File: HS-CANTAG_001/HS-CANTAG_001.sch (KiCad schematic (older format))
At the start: 20 parts, among them Y1 16MHz

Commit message: ・CANTAG回路図編集
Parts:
- removed J?: B5B-XH-A_LF__SN_, digikey-footprints:PinHeader_1x5_P2.5mm_Drill1.1mm, symbol dk_Rectangular-Connectors-Headers-Male-Pins:B5B-XH-A_LF__SN_
- added C6, C9: 100uf, symbol Device:C
- added C7, C8: 0.1uf, symbol Device:C
- added D1: 5A, Diode_THT:D_DO-41_SOD81_P10.16mm_Horizontal, symbol Diode:SB160
- added J?: B4B-XH-A_LF__SN_, digikey-footprints:PinHeader_1x4_P2.5mm_Drill1.1mm, symbol dk_Rectangular-Connectors-Headers-Male-Pins:B4B-XH-A_LF__SN_
- added J?: Jack-DC, symbol Connector:Jack-DC
- added SW?: SW_Push, symbol Switch:SW_Push
- added U?: R-78E5.0-0.5, Converter_DCDC:Converter_DCDC_RECOM_R-78E-0.5_THT, symbol Regulator_Switching:R-78E5.0-0.5
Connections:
- wire segments 84 -> 104
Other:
- moved on the sheet: C1, C2, C3, C4, C5, CAN_H, D1, J?, JP?, R1, R2, R3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

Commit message: ・CAN回路更新
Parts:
- removed J?: Jack-DC, symbol Connector:Jack-DC
- added J3: Barrel_Jack, digikey-footprints:Barrel_Jack_5.5mmODx2.1mmID_PJ-202A, symbol Connector:Barrel_Jack_Switch
- C1, C2, C5, C7, C8: footprint (none) -> Capacitor_SMD:C_1206_3216Metric
- C3, C4: footprint (none) -> Capacitor_THT:C_Disc_D4.3mm_W1.9mm_P5.00mm
- C6, C9: footprint (none) -> Capacitor_THT:CP_Radial_D6.3mm_P2.50mm
- CAN_H1: renamed from CAN_H; footprint digikey-footprints:PinHeader_1x2_P2mm_Drill1mm -> Connector_PinSocket_2.54mm:PinSocket_1x02_P2.54mm_Vertical
- D1: footprint (none) -> digikey-footprints:LED_3mm_Radial
- J1: renamed from J?; footprint digikey-footprints:PinHeader_1x2_P2mm_Drill1mm -> Connector_PinHeader_2.54mm:PinHeader_1x02_P2.54mm_Vertical
- J2: renamed from J?; footprint digikey-footprints:PinHeader_1x4_P2.5mm_Drill1.1mm -> Connector_PinHeader_2.54mm:PinHeader_1x04_P2.54mm_Vertical
- J4, J5: renamed from J?; footprint digikey-footprints:PinHeader_1x4_P2.5mm_Drill1.1mm -> Connector_Hirose:Hirose_DF63-4P-3.96DSA_1x04_P3.96mm_Horizontal
- JP1: renamed from JP?; footprint (none) -> Connector_PinHeader_2.54mm:PinHeader_1x02_P2.54mm_Vertical
- R1, R2, R3, R4: footprint (none) -> Resistor_THT:R_Axial_DIN0204_L3.6mm_D1.6mm_P7.62mm_Horizontal
- SW1: renamed from SW?; footprint (none) -> digikey-footprints:Switch_Tactile_THT_B3F-1xxx
- U1: renamed from U?; footprint (none) -> hotsprings-footprints:MCP2515_SMD
- U3: renamed from U?; footprint (none) -> hotsprings-footprints:MCP2551_SMD
- Y1: footprint (none) -> Crystal:Crystal_HC49-4H_Vertical
- gave numbers to parts that had none: 1
- renumbered D1 to D2
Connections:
- wire segments 104 -> 105
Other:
- note added: "Power"
- moved on the sheet: C1, C2, C3, C4, C5, C6, C7, C8, C9, CAN_H1, D1, D2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

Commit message: ・回路修正
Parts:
- J4, J5: footprint Connector_Hirose:Hirose_DF63-4P-3.96DSA_1x04_P3.96mm_Horizontal -> Connector_JST:JST_VH_B4P-VH-B_1x04_P3.96mm_Vertical
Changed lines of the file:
@@
 F 0 "J4" V 4991 3172 50  0000 R CNN
 F 1 "CAN1" V 4900 3172 50  0000 R CNN
-F 2 "Connector_Hirose:Hirose_DF63-4P-3.96DSA_1x04_P3.96mm_Horizontal" H 5000 3500 60  0001 L CNN
+F 2 "Connector_JST:JST_VH_B4P-VH-B_1x04_P3.96mm_Vertical" H 5000 3500 60  0001 L CNN
 F 3 "http://www.jst-mfg.com/product/pdf/eng/eXH.pdf" H 5000 3600 60  0001 L CNN
 F 4 "455-2249-ND" H 5000 3700 60  0001 L CNN "Digi-Key_PN"
@@
 F 0 "J5" V 4991 3772 50  0000 R CNN
 F 1 "CAN2" V 4900 3772 50  0000 R CNN
-F 2 "Connector_Hirose:Hirose_DF63-4P-3.96DSA_1x04_P3.96mm_Horizontal" H 5000 4100 60  0001 L CNN
+F 2 "Connector_JST:JST_VH_B4P-VH-B_1x04_P3.96mm_Vertical" H 5000 4100 60  0001 L CNN
 F 3 "http://www.jst-mfg.com/product/pdf/eng/eXH.pdf" H 5000 4200 60  0001 L CNN
 F 4 "455-2249-ND" H 5000 4300 60  0001 L CNN "Digi-Key_PN"

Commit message: ・CAN回路更新
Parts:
- removed U1: MCP2515, hotsprings-footprints:MCP2515_SMD, symbol HotSprings:MCP2515
- added U1: MCP2515_SMD18p, hotsprings-footprints:MCP2515_SMD(18p), symbol HotSprings:MCP2515_SMD18p
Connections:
- net +5V: now also U1.18 (VDD)
- net GNDPWR: now also U1.9 (VSS)
- net at U3.1 (TXD): now also U1.1 (TXCAN)
- net at D1.2 (A): now also U1.11 (RX0BF)
- net at J2.1, RN1.2 (R1): now also U1.13 (SCK)
- net at J2.2, RN1.3 (R2): now also U1.14 (SI)
- net at J2.3, RN1.4 (R3): now also U1.15 (SO)
- net at J2.4, RN1.5 (R4): now also U1.16 (CS)
- net at R1.2, SW1.2: now also U1.17 (RESET)
- net at U3.4 (RXD): now also U1.2 (RXCAN)
- net at C3.1, Y1.1: now also U1.7 (OSC2)
- net at C4.1, Y1.2: now also U1.8 (OSC1)
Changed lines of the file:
@@
 CAN
-$Comp
-L HotSprings:MCP2515 U1
-U 1 1 5D287E4C
-P 2050 2400
-F 0 "U1" H 2050 3075 50  0000 C CNN
-F 1 "MCP2515" H 2050 2984 50  0000 C CNN
-F 2 "hotsprings-footprints:MCP2515_SMD" H 2050 2950 50  0001 C CNN
-F 3 "" H 2050 2950 50  0001 C CNN
-	1    2050 2400
-	1    0    0    -1
-$EndComp
 $Comp
 L HotSprings:MCP2551 U3
@@
 	2550 2050 2550 1700
 Wire Wire Line
-	2550 2550 2450 2550
-Wire Wire Line
 	2600 2350 2450 2350
 Wire Wire Line
@@
 Wire Wire Line
 	2700 2150 2450 2150
-Wire Wire Line
-	2450 2750 2500 2750
-Wire Wire Line
-	2500 2750 2500 3200
 Wire Wire Line
 	2900 2750 2900 2450
@@
 Wire Wire Line
 	1150 2200 1150 2500
-Wire Wire Line
-	1650 2650 1500 2650
-Wire Wire Line
-	1500 2650 1500 2500
-Wire Wire Line
-	1500 2500 1150 2500
 Connection ~ 1150 2500
-Wire Wire Line
-	1400 2550 1400 2750
-Wire Wire Line
-	1400 2750 1650 2750
 Wire Wire Line
 	800  2800 1000 2800
@@
 	950  2500 950  2550
 Connection ~ 800  2500
-Wire Wire Line
-	950  2550 1400 2550
 $Comp
 L power:GNDPWR #PWR0113
@@
 $EndComp
 $Comp
-L Device:C C6
-U 1 1 5D364A2E
-P 2100 5700
-F 0 "C6" H 2215 5746 50  0000 L CNN
-F 1 "100uf" H 2215 5655 50  0000 L CNN
-F 2 "Capacitor_THT:CP_Radial_D6.3mm_P2.50mm" H 2138 5550 50  0001 C CNN
-F 3 "~" H 2100 5700 50  0001 C CNN
-	1    2100 5700
-	-1   0    0    1
-$EndComp
-$Comp
 L Device:C C7
 U 1 1 5D365638
@@
 	-1   0    0    1
 $EndComp
-Wire Wire Line
-	2100 5550 2550 5550
 Connection ~ 2550 5550
 Wire Wire Line
@@
 	3050 5850 2550 5850
 Connection ~ 2550 5850
-Wire Wire Line
-	2550 5850 2100 5850
-Connection ~ 2100 5850
-Wire Wire Line
-	2100 5850 1800 5850
 $Comp
 L Diode:SB160 D2
@@
 Wire Wire Line
 	2000 5350 2000 5550
-Wire Wire Line
-	2000 5550 2100 5550
-Connection ~ 2100 5550
 Text Notes 700  5100 0    50   ~ 0
 Power
@@
 $EndComp
 Wire Wire Line
-	2550 2550 2550 4100
-Wire Wire Line
 	2600 2350 2600 4200
 Wire Wire Line
@@
 	1600 5650 1600 5750
 Connection ~ 1600 5750
+$Comp
+L HotSprings:MCP2515_SMD18p U1
+U 1 1 5D2C910C
+P 2050 2400
+F 0 "U1" H 2050 3075 50  0000 C CNN
+F 1 "MCP2515_SMD18p" H 2050 2984 50  0000 C CNN
+F 2 "hotsprings-footprints:MCP2515_SMD(18p)" H 2050 2950 50  0001 C CNN
+F 3 "" H 2050 2950 50  0001 C CNN
+	1    2050 2400
+	1    0    0    -1
+$EndComp
+Wire Wire Line
+	1500 2550 1500 2650
+Wire Wire Line
+	1500 2650 1650 2650
+Wire Wire Line
+	950  2550 1500 2550
+Wire Wire Line
+	1550 2500 1550 2550
+Wire Wire Line
+	1550 2550 1650 2550
+Wire Wire Line
+	1150 2500 1550 2500
+Connection ~ 2100 5550
+Connection ~ 2100 5850
+Wire Wire Line
+	2100 5850 1800 5850
+Wire Wire Line
+	2550 5850 2100 5850
+Wire Wire Line
+	2000 5550 2100 5550
+Wire Wire Line
+	2100 5550 2550 5550
+$Comp
+L Device:C C6
+U 1 1 5D364A2E
+P 2100 5700
+F 0 "C6" H 2215 5746 50  0000 L CNN
+F 1 "100uf" H 2215 5655 50  0000 L CNN
+F 2 "Capacitor_THT:CP_Radial_D6.3mm_P2.50mm" H 2138 5550 50  0001 C CNN
+F 3 "~" H 2100 5700 50  0001 C CNN
+	1    2100 5700
+	-1   0    0    1
+$EndComp
+Wire Wire Line
+	1650 2750 1650 2850
+Wire Wire Line
+	2550 2450 2450 2450
+Wire Wire Line
+	2550 2450 2550 4100
+Wire Wire Line
+	2450 2650 2500 2650
+Wire Wire Line
+	2500 2650 2500 3200
 $EndSCHEMATC

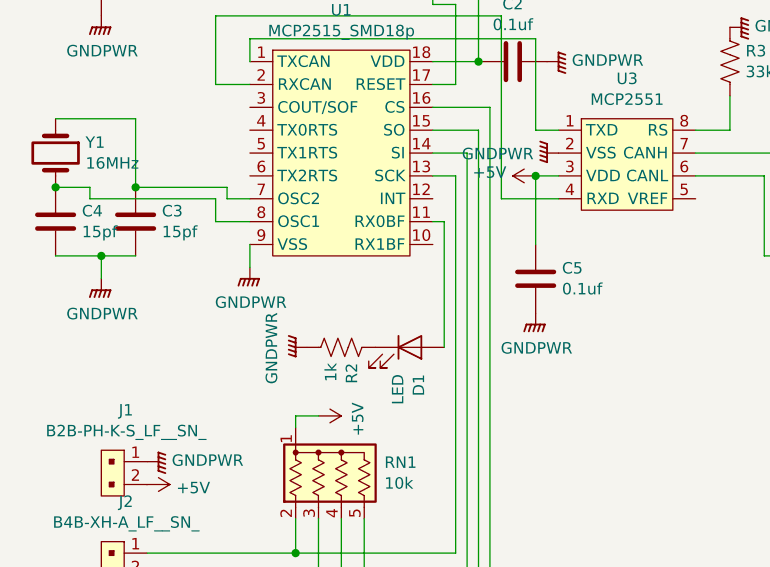
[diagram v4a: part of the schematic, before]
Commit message: ・CANTAG外形データの追加
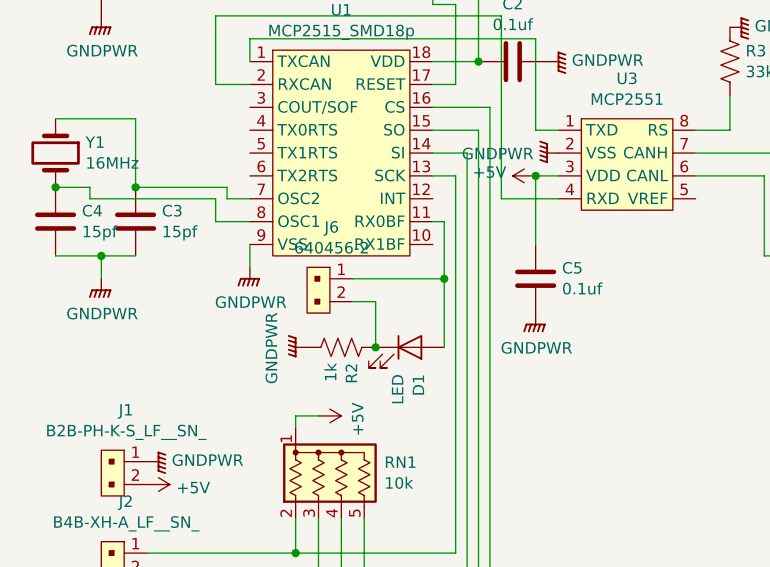
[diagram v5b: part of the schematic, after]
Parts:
- added J6: 640456-2, digikey-footprints:PinHeader_1x2_P2.54mm_Drill1.02mm, symbol dk_Rectangular-Connectors-Headers-Male-Pins:640456-2
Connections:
- net at D1.1 (K), R2.1: now also J6.2
- net at D1.2 (A), U1.11 (RX0BF): now also J6.1
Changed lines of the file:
@@
 Wire Wire Line
 	2450 2650 2500 2650
+$Comp
+L dk_Rectangular-Connectors-Headers-Male-Pins:640456-2 J6
+U 1 1 5D2E5892
+P 2000 2900
+F 0 "J6" V 1775 2908 50  0000 C CNN
+F 1 "640456-2" V 1866 2908 50  0000 C CNN
+F 2 "digikey-footprints:PinHeader_1x2_P2.54mm_Drill1.02mm" H 2200 3100 60  0001 L CNN
+F 3 "https://www.te.com/commerce/DocumentDelivery/DDEController?Action=srchrtrv&DocNm=640456&DocType=Customer+Drawing&DocLang=English" H 2200 3200 60  0001 L CNN
+F 4 "A1921-ND" H 2200 3300 60  0001 L CNN "Digi-Key_PN"
+F 5 "640456-2" H 2200 3400 60  0001 L CNN "MPN"
+F 6 "Connectors, Interconnects" H 2200 3500 60  0001 L CNN "Category"
+F 7 "Rectangular Connectors - Headers, Male Pins" H 2200 3600 60  0001 L CNN "Family"
+F 8 "https://www.te.com/commerce/DocumentDelivery/DDEController?Action=srchrtrv&DocNm=640456&DocType=Customer+Drawing&DocLang=English" H 2200 3700 60  0001 L CNN "DK_Datasheet_Link"
+F 9 "/product-detail/en/te-connectivity-amp-connectors/640456-2/A1921-ND/109003" H 2200 3800 60  0001 L CNN "DK_Detail_Page"
+F 10 "CONN HEADER VERT 2POS 2.54MM" H 2200 3900 60  0001 L CNN "Description"
+F 11 "TE Connectivity AMP Connectors" H 2200 4000 60  0001 L CNN "Manufacturer"
+F 12 "Active" H 2200 4100 60  0001 L CNN "Status"
+	1    2000 2900
+	0    1    1    0
+$EndComp
 Wire Wire Line
-	2500 2650 2500 3200
+	2100 2900 2500 2900
+Wire Wire Line
+	2500 2650 2500 2900
+Connection ~ 2500 2900
+Wire Wire Line
+	2500 2900 2500 3200
+Wire Wire Line
+	2100 3000 2200 3000
+Wire Wire Line
+	2200 3000 2200 3200
+Connection ~ 2200 3200
 $EndSCHEMATC
